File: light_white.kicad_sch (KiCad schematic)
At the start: 37 parts, among them Q1 Si2319CDS, U8 TPS61181ARTER

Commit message: cinna 4 more circuit
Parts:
- added C18, C19: C4u7, symbol Device:C
- added C20: C100n, symbol Device:C
- added C21, C22, C23, C24, C25: C1u, symbol Device:C
- added D20, D33, D34, D35, D36, D37, D38, D39, D40, D41, D42, D43, D44, D45, D46, D47, D48, D49, D50, D51: LED, symbol Device:LED
- added D22: D_Schottky, symbol Device:D_Schottky
- added D3: US1A, Diode_SMD:D_SMA, symbol Diode:US1A
- added L3: L, symbol Device:L
- added Q2: Si2319CDS, Package_TO_SOT_SMD:SOT-23, symbol Transistor_FET:Si2319CDS
- added R12, R14, R16: R, symbol Device:R
- added TP2: TestPoint, symbol Connector:TestPoint
- added U1: TPS61181ARTER, RTE16_1P7X1P7, symbol -TPS61181ARTER:TPS61181ARTER
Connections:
- net GND: now also C18.2, C19.2, C20.2, C21.2, C22.2, C23.2, C24.2, C25.2, D3.2 (A), R16.1, U1.1 (PGND), U1.10 (GND), U1.17 (EPAD)
- net cin: now also C20.1, U1.6 (CIN)
- net en: now also U1.15 (EN)
- net fault: now also U1.16 (FAULT)
- net hc_strip_1: now also D41.1 (K)
- net hc_strip_2: now also D51.1 (K)
- net led_vcc: now also D3.1 (K), L3.1, Q2.2 (S)
- net sw: now also D22.2 (A), L3.2, U1.2 (SW)
- net vbat: now also C21.1, R14.2, U1.3 (VBAT)
- net vbus: now also C18.1, C19.1, Q2.3 (D), R12.1, R14.1
- net vo: now also C22.1, C23.1, C24.1, C25.1, D22.1 (K), U1.4 (VO)
- new net: U1.12 (IFB4), U1.13 (IFB5), U1.14 (IFB6)
- new net: R16.2, U1.5 (ISET)
- new net: U1.7 (IFB1), U1.8 (IFB2)
- new net: D43.1 (K), D44.2 (A)
- new net: D42.1 (K), D43.2 (A)
- new net: D37.1 (K), D38.2 (A)
- new net: D36.1 (K), D37.2 (A)
- new net: D50.1 (K), D51.2 (A)
- new net: D49.1 (K), D50.2 (A)
- new net: D47.1 (K), D48.2 (A)
- new net: D46.1 (K), D47.2 (A)
- new net: D45.1 (K), D46.2 (A)
- new net: D44.1 (K), D45.2 (A)
- new net: D40.1 (K), D41.2 (A)
- new net: D39.1 (K), D40.2 (A)
- new net: D48.1 (K), D49.2 (A)
- new net: D33.1 (K), D34.2 (A)
- new net: D20.1 (K), D33.2 (A)
- new net: D34.1 (K), D35.2 (A)
- new net: D35.1 (K), D36.2 (A)
- new net: D38.1 (K), D39.2 (A)
- new net: D20.2 (A), D42.2 (A)
- new net: Q2.1 (G), R12.2
- new net pwn: TP2.1, U1.11 (DCTRL)
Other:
- note added: "Total drive power ~= 2.95V x 60mA x 20 = 3.54W whatever that means"
- note added: "string/CH = 3mA"

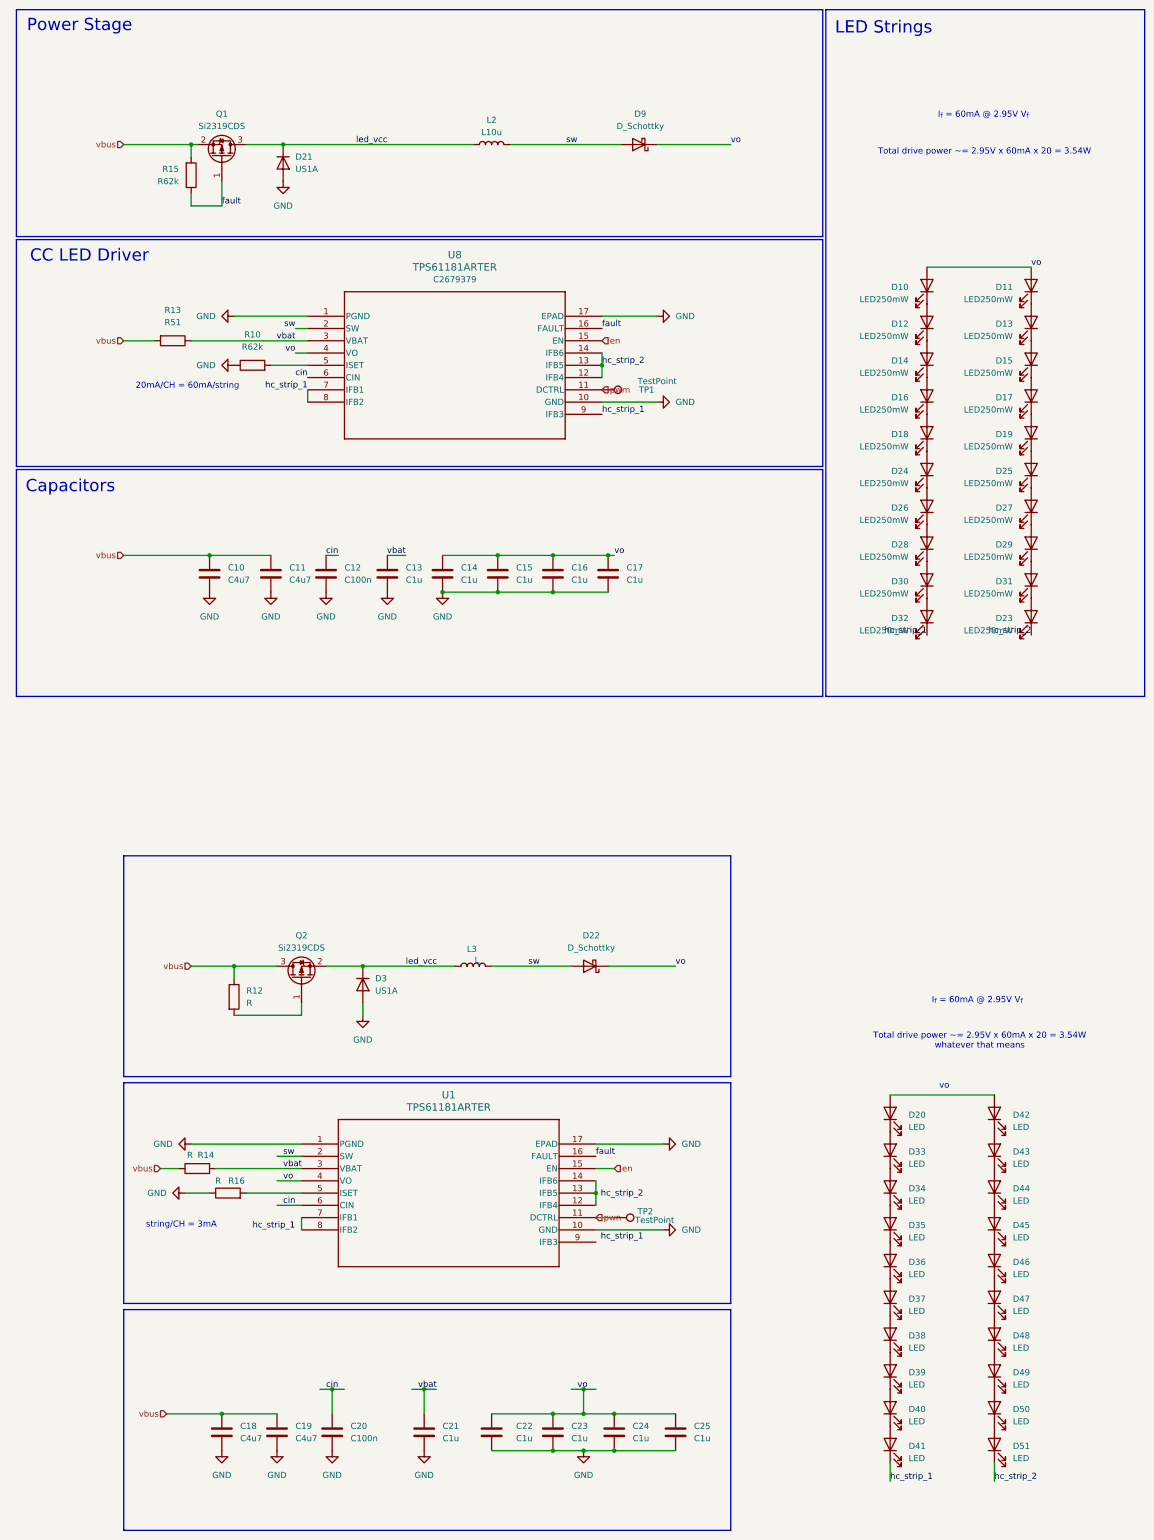
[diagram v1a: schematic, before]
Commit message: Cleanup, add 5vREG block
Signed-off-by: sanyue <sanyue7th@gmail.com>
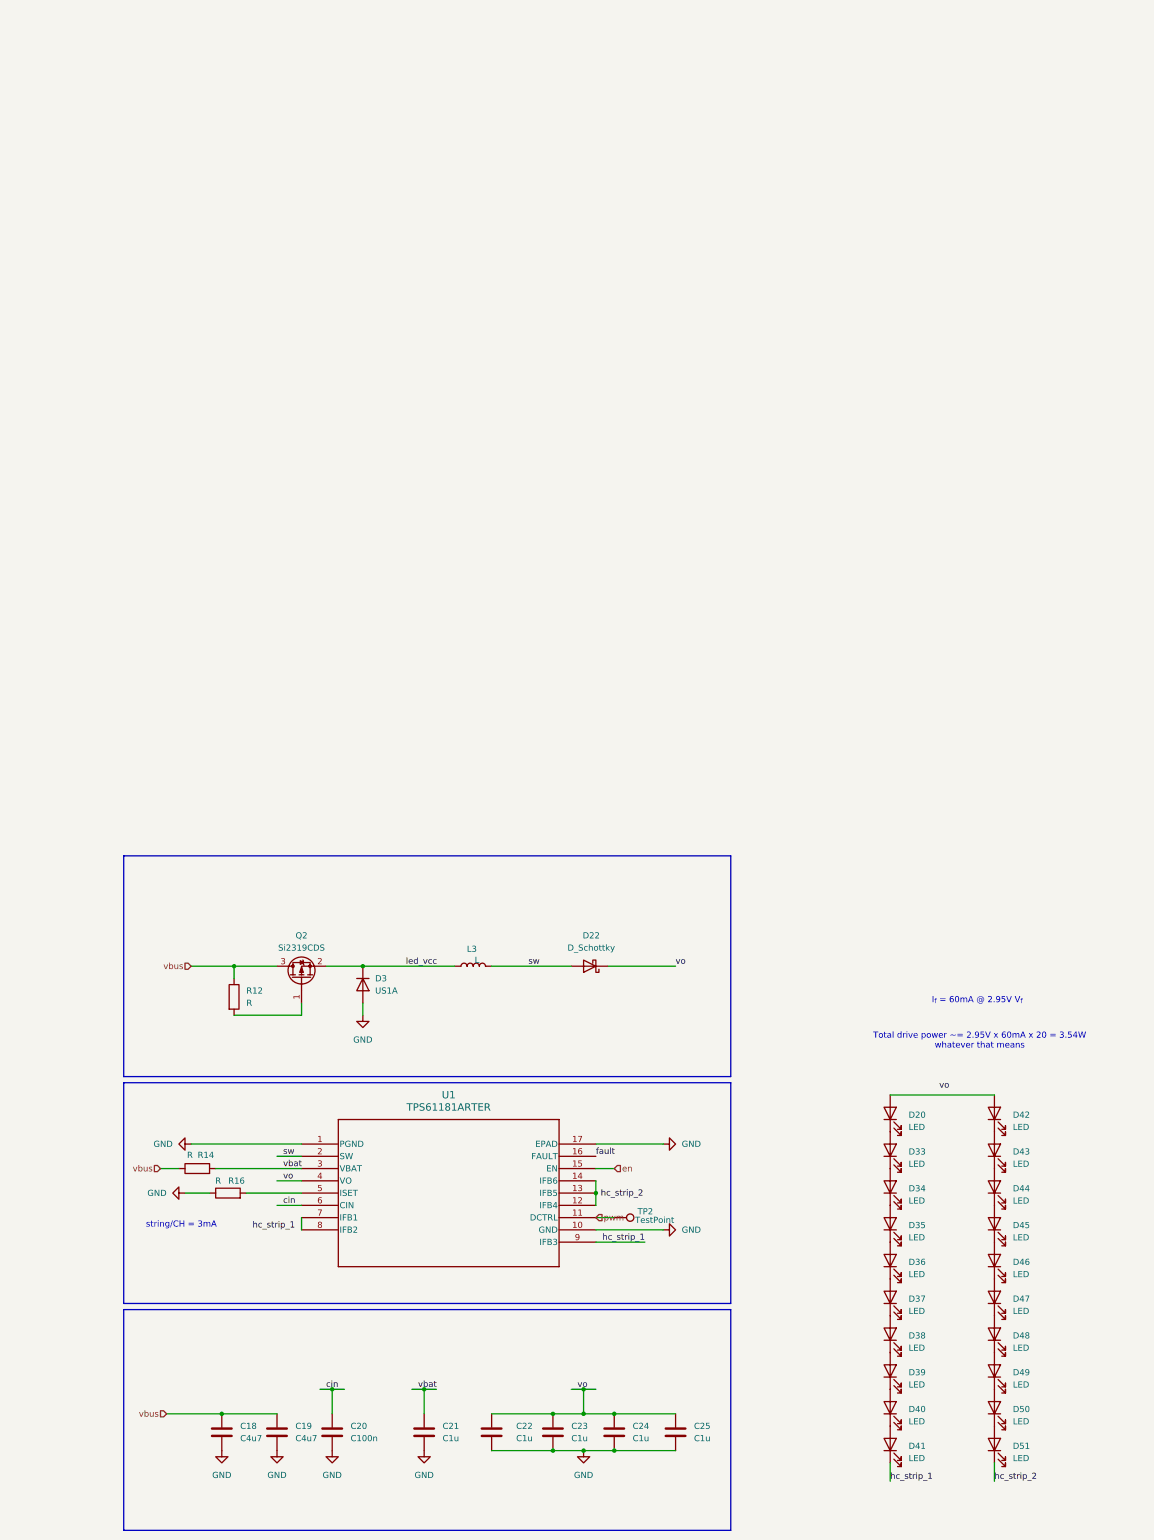
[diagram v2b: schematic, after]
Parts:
- removed C10, C11: C4u7, Capacitor_SMD:C_0603_1608Metric, symbol Device:C
- removed C12: C100n, Capacitor_SMD:C_0402_1005Metric, symbol Device:C
- removed C13, C14, C15, C16, C17: C1u, Capacitor_SMD:C_0402_1005Metric, symbol Device:C
- removed D10, D11, D12, D13, D14, D15, D16, D17, D18, D19, D23, D24, D25, D26, D27, D28, D29, D30, D31, D32: LED250mW, aaaafootprintlib:LED_EAHC2835WD6, symbol Device:LED
- removed D21: US1A, Diode_SMD:D_SMA, symbol Diode:US1A
- removed D9: D_Schottky, Diode_SMD:D_SOD-123, symbol Device:D_Schottky
- removed L2: L10u, Inductor_SMD:L_Changjiang_FNR5040S, symbol Device:L
- removed Q1: Si2319CDS, Package_TO_SOT_SMD:SOT-23, symbol Transistor_FET:Si2319CDS
- removed R10, R15: R62k, Resistor_SMD:R_0402_1005Metric, symbol Device:R
- removed R13: R51, Resistor_SMD:R_0402_1005Metric, symbol Device:R
- removed TP1: TestPoint, TestPoint:TestPoint_Pad_D1.0mm, symbol Connector:TestPoint
- removed U8: TPS61181ARTER, aaaafootprintlib:RTE16_1P7X1P7, symbol aaasymlib:TPS61181ARTER
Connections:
- net pwn is gone; now on net pwm: TP2.1, U1.11 (DCTRL)
- net hc_strip_1: now also U1.9 (IFB3)
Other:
- note removed: "20mA/CH = 60mA/string"
- note removed: "CC LED Driver"
- note removed: "Capacitors"
- note removed: "LED Strings"
- note removed: "Power Stage"
- note removed: "Total drive power ~= 2.95V x 60mA x 20 = 3.54W"
